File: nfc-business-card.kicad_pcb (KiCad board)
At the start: 2 copper layers, 89 x 51 mm, 9 parts, among them U1 NT3H2111W0FHKH

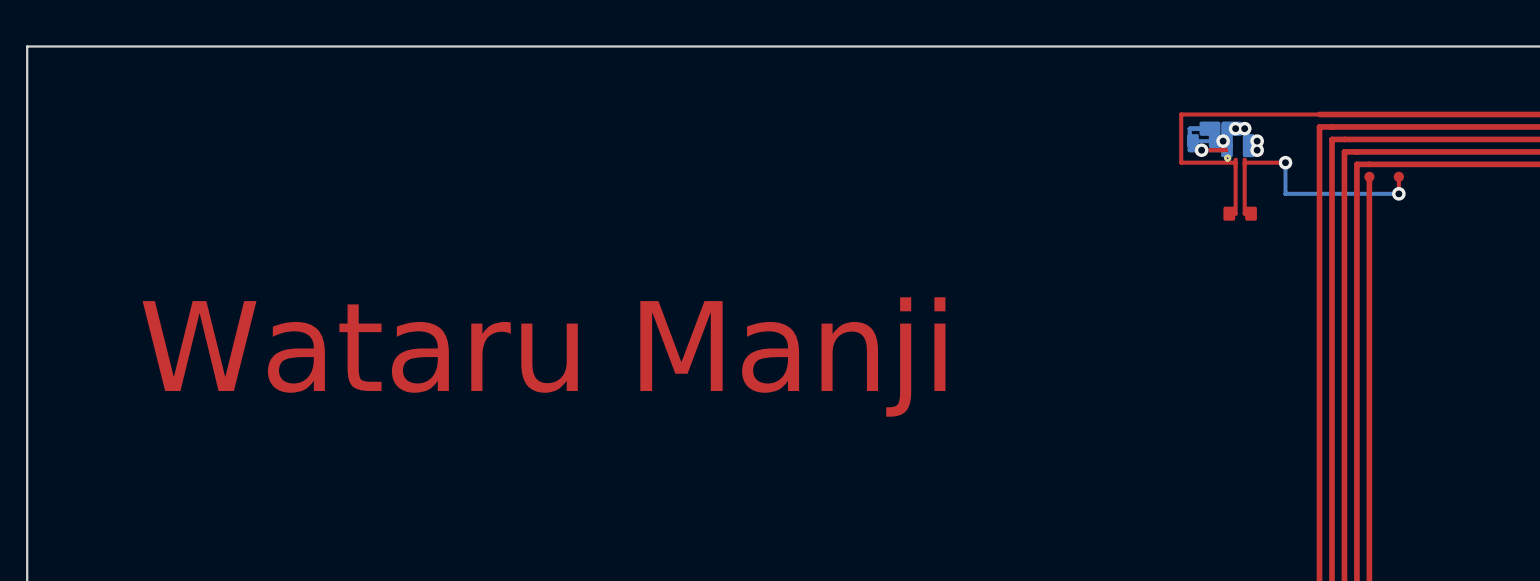
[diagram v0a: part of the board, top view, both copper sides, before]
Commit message: feat(design): real-board preview fidelity and Georgia Bold ENIG name
- LA/LB feeds at 0.25 mm (match antenna) and rendered under-mask in preview
- Preview draws net-tie pads, tented vias, GND island, B.Cu hints
- Name font switched to Georgia Bold (em 5.1 mm) via split_font.py
  (unique 'GeorgiaBold' family resolves in KiCad; system-registered)
- fontconfig config wired into pcbnow bake and kicad-cli fab exports
- fonttools dep for font splitting
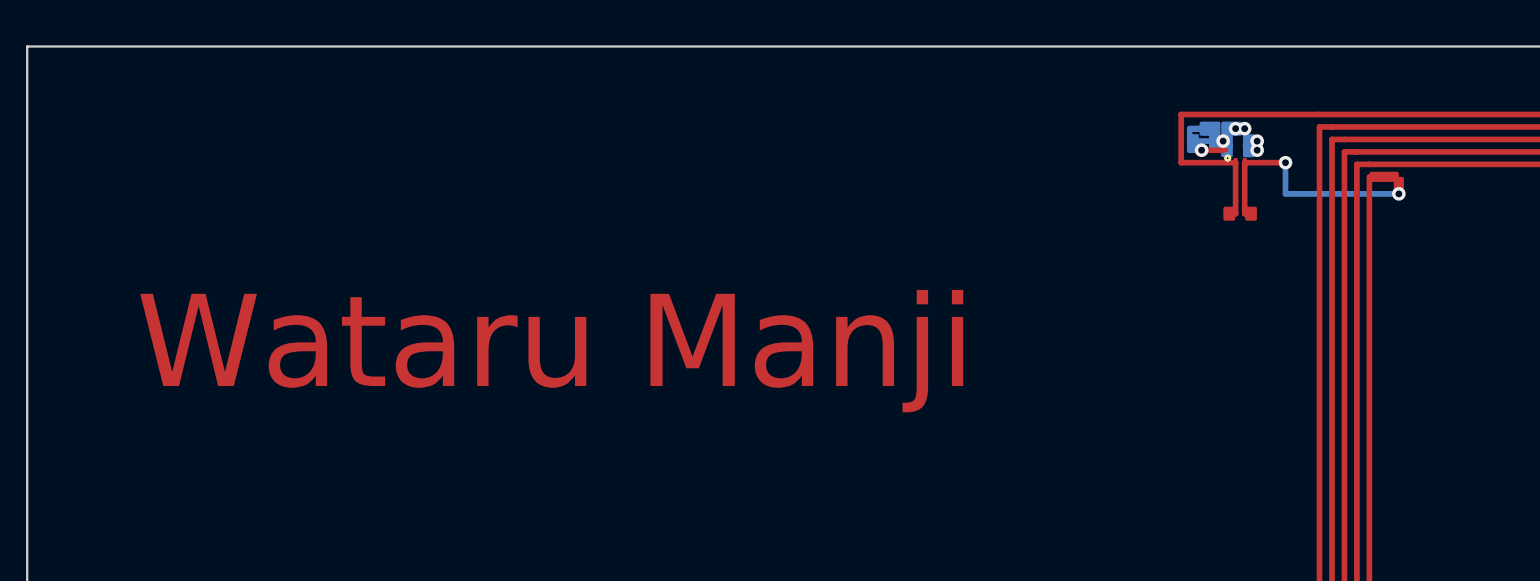
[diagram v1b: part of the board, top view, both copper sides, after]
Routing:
- net LB: track 11.5 -> 10.7 mm

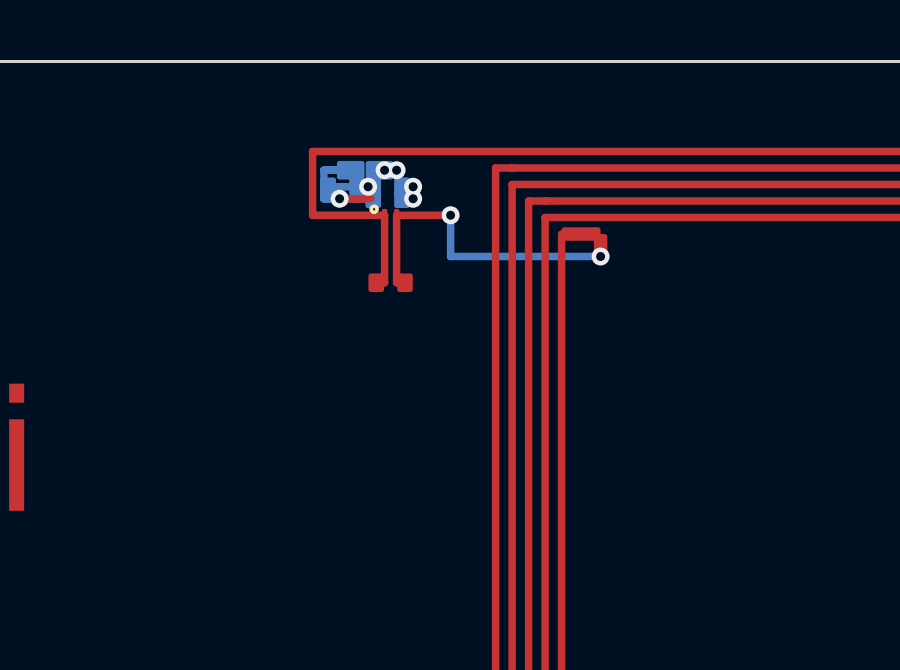
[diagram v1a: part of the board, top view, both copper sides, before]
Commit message: fix: route LB under LA skirt without shorting VOUT
Keep the westbound VOUT crossing on F.Cu above the LA skirt, and drop
to B.Cu only in the clearance column between VCC and VOUT. Lower the
KiCad min track width to the JLC floor so intentional 0.15 mm NC stubs
pass DRC.
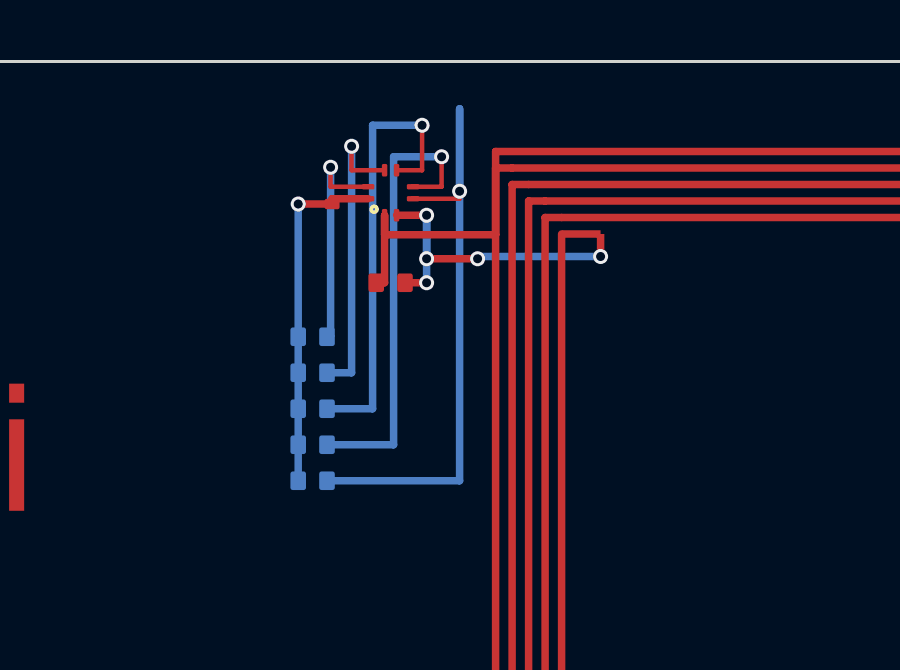
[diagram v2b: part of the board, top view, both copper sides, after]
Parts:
- moved R6 9.73 mm to (50.9, 14.0)
- moved R5 8.96 mm to (50.9, 12.8)
- moved R3 8.19 mm to (50.9, 11.6)
- moved R4 6.93 mm to (50.9, 10.4)
- moved R2 5.10 mm to (50.9, 9.18)
- moved GND1 0.31 mm to (51.5, 4.75)
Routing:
- net VOUT: track 0.37 -> 21.4 mm
- net VCC: track 0.37 -> 15.4 mm
- net SDA: track 0.37 -> 15.0 mm
- net FD: track 0.37 -> 10.3 mm
- net SCL: track 0.37 -> 7.67 mm
- net GND: track 7.65 -> 11.7 mm
- net LA: track 708.6 -> 705.1 mm
- net LB: track 10.7 -> 11.3 mm, vias 2 -> 5

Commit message: fix: detach LA feed from antenna left-edge short
Step the LA feed west off the spiral start before rising so it no
longer T-junctions onto the outer left turn and shorts turn 1. Guard
the regression in check_layout and refresh fab outputs.
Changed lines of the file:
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@@
 	(segment
 		(start 57 3)
-		(end 57 5.775)
+		(end 56.55 3)
 		(width 0.25)
 		(layer "F.Cu")
@@
 	)
 	(segment
-		(start 57 5.775)
+		(start 56.55 3)
+		(end 56.55 5.775)
+		(width 0.25)
+		(layer "F.Cu")
+		(net "LA")
+	)
+	(segment
+		(start 56.55 5.775)
 		(end 53.3 5.775)
 		(width 0.25)

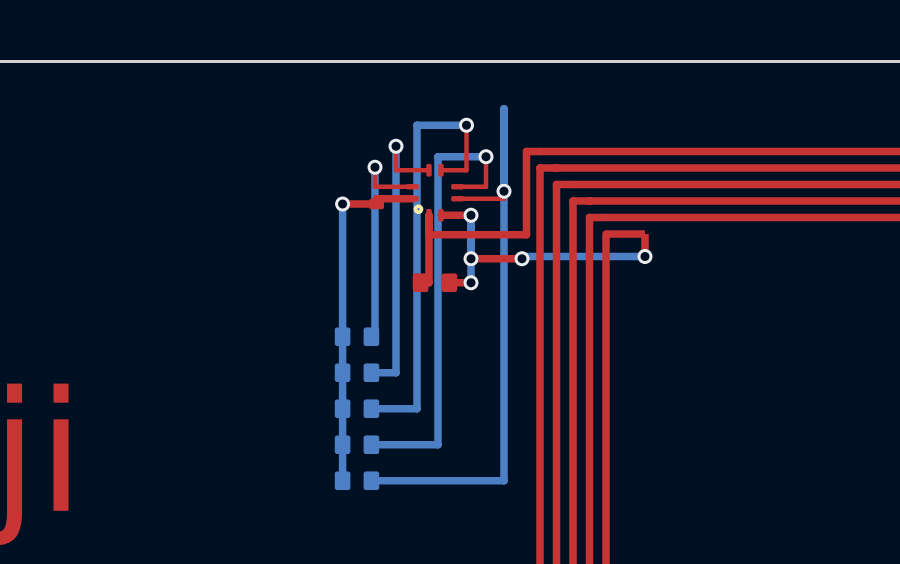
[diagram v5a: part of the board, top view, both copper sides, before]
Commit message: refactor: widen LA/LB bus gap and keep schematic R bank off the U1 body
- FEED_BUS_W_MM=0.18 (XQFN ROW) on the 0.40 mm-pitch bus columns:
  parallel pair gap 0.15 -> 0.22 mm, still antenna width elsewhere, no
  width step at the XQFN pads
- schematic R2-R6 columns moved outside the U1 symbol body so no vertical
  or jog crosses the rectangle; net labels on the outward jog/stub
- second GND symbol (#PWR02) on the rail's right end; title-block date
  now generated at write time
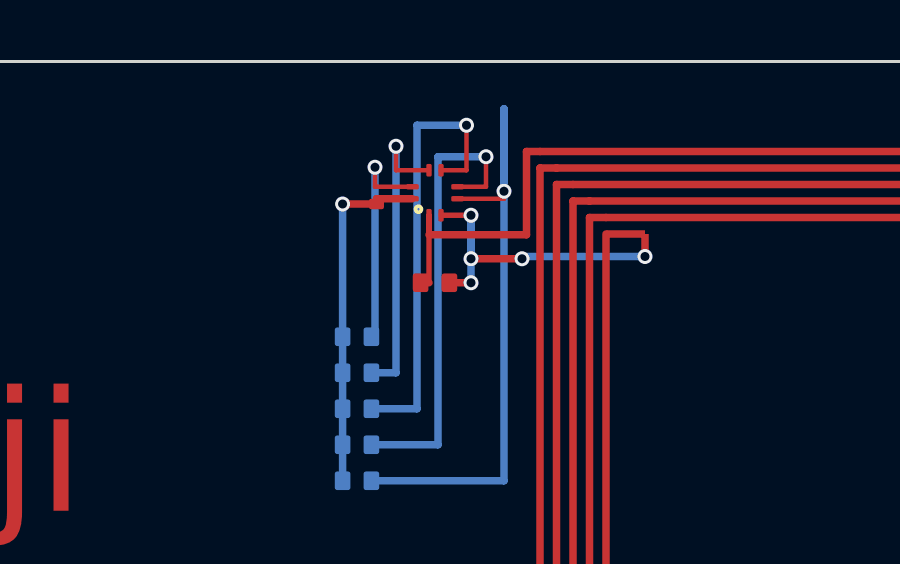
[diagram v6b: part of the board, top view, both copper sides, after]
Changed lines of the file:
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@@
 		(start 53.3 5.775)
 		(end 53.3 5.125)
-		(width 0.25)
+		(width 0.18)
 		(layer "F.Cu")
 		(net "LA")
@@
 		(start 53.3 7.375)
 		(end 53.3 5.125)
-		(width 0.25)
+		(width 0.18)
 		(layer "F.Cu")
 		(net "LA")
@@
 		(start 54.7 5.125)
 		(end 53.7 5.125)
-		(width 0.25)
+		(width 0.18)
 		(layer "F.Cu")
 		(net "LB")
